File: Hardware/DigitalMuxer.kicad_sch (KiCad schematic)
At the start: 23 parts, among them SW1 Push_Button, SW2 Push_Button, SW3 Push_Button, SW4 Push_Button, SW5 Slide Switch, U2 PCF8574

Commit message: Use tags for nets, apply netgroups, mess around in pcb view
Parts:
- C10, C8, C9: footprint (none) -> Capacitor_SMD:C_0201_0603Metric
- D1, D2, D3: footprint (none) -> LED_SMD:LED_0201_0603Metric
- R10, R11, R12, R13, R3, R4, R5, R6, R7, R8, R9: footprint Resistor_THT:R_Axial_DIN0207_L6.3mm_D2.5mm_P10.16mm_Horizontal -> Resistor_SMD:R_0201_0603Metric
- U2: footprint (none) -> Snapeda:DW16
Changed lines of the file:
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@@
 			)
 		)
-		(property "Footprint" "Resistor_THT:R_Axial_DIN0207_L6.3mm_D2.5mm_P10.16mm_Horizontal"
+		(property "Footprint" "Resistor_SMD:R_0201_0603Metric"
 			(at 136.652 50.419 0)
 			(effects
@@
 			)
 		)
-		(property "Footprint" ""
+		(property "Footprint" "Snapeda:DW16"
 			(at 99.06 68.58 0)
 			(effects
@@
 			)
 		)
-		(property "Footprint" "Resistor_THT:R_Axial_DIN0207_L6.3mm_D2.5mm_P10.16mm_Horizontal"
+		(property "Footprint" "Resistor_SMD:R_0201_0603Metric"
 			(at 134.112 83.439 0)
 			(effects
@@
 			)
 		)
-		(property "Footprint" "Resistor_THT:R_Axial_DIN0207_L6.3mm_D2.5mm_P10.16mm_Horizontal"
+		(property "Footprint" "Resistor_SMD:R_0201_0603Metric"
 			(at 134.112 145.669 0)
 			(effects
@@
 			)
 		)
-		(property "Footprint" ""
+		(property "Footprint" "Capacitor_SMD:C_0201_0603Metric"
 			(at 111.4552 35.56 0)
 			(effects
@@
 			)
 		)
-		(property "Footprint" "Resistor_THT:R_Axial_DIN0207_L6.3mm_D2.5mm_P10.16mm_Horizontal"
+		(property "Footprint" "Resistor_SMD:R_0201_0603Metric"
 			(at 145.542 50.419 0)
 			(effects
@@
 			)
 		)
-		(property "Footprint" "Resistor_THT:R_Axial_DIN0207_L6.3mm_D2.5mm_P10.16mm_Horizontal"
+		(property "Footprint" "Resistor_SMD:R_0201_0603Metric"
 			(at 181.102 50.419 0)
 			(effects
@@
 			)
 		)
-		(property "Footprint" "Resistor_THT:R_Axial_DIN0207_L6.3mm_D2.5mm_P10.16mm_Horizontal"
+		(property "Footprint" "Resistor_SMD:R_0201_0603Metric"
 			(at 172.212 50.419 0)
 			(effects
@@
 			)
 		)
-		(property "Footprint" ""
+		(property "Footprint" "LED_SMD:LED_0201_0603Metric"
 			(at 172.72 60.96 90)
 			(effects
@@
 			)
 		)
-		(property "Footprint" ""
+		(property "Footprint" "Capacitor_SMD:C_0201_0603Metric"
 			(at 121.6152 35.56 0)
 			(effects
@@
 			)
 		)
-		(property "Footprint" "Resistor_THT:R_Axial_DIN0207_L6.3mm_D2.5mm_P10.16mm_Horizontal"
+		(property "Footprint" "Resistor_SMD:R_0201_0603Metric"
 			(at 154.432 50.419 0)
 			(effects
@@
 			)
 		)
-		(property "Footprint" "Resistor_THT:R_Axial_DIN0207_L6.3mm_D2.5mm_P10.16mm_Horizontal"
+		(property "Footprint" "Resistor_SMD:R_0201_0603Metric"
 			(at 134.112 98.679 0)
 			(effects
@@
 			)
 		)
-		(property "Footprint" "Resistor_THT:R_Axial_DIN0207_L6.3mm_D2.5mm_P10.16mm_Horizontal"
+		(property "Footprint" "Resistor_SMD:R_0201_0603Metric"
 			(at 134.112 113.919 0)
 			(effects
@@
 			)
 		)
-		(property "Footprint" "Resistor_THT:R_Axial_DIN0207_L6.3mm_D2.5mm_P10.16mm_Horizontal"
+		(property "Footprint" "Resistor_SMD:R_0201_0603Metric"
 			(at 163.322 50.419 0)
 			(effects
@@
 			)
 		)
-		(property "Footprint" "Resistor_THT:R_Axial_DIN0207_L6.3mm_D2.5mm_P10.16mm_Horizontal"
+		(property "Footprint" "Resistor_SMD:R_0201_0603Metric"
 			(at 134.112 130.429 0)
 			(effects
@@
 			)
 		)
-		(property "Footprint" ""
+		(property "Footprint" "LED_SMD:LED_0201_0603Metric"
 			(at 181.61 63.5 90)
 			(effects
@@
 			)
 		)
-		(property "Footprint" ""
+		(property "Footprint" "Capacitor_SMD:C_0201_0603Metric"
 			(at 102.5652 35.56 0)
 			(effects
@@
 			)
 		)
-		(property "Footprint" ""
+		(property "Footprint" "LED_SMD:LED_0201_0603Metric"
 			(at 163.83 58.42 90)
 			(effects

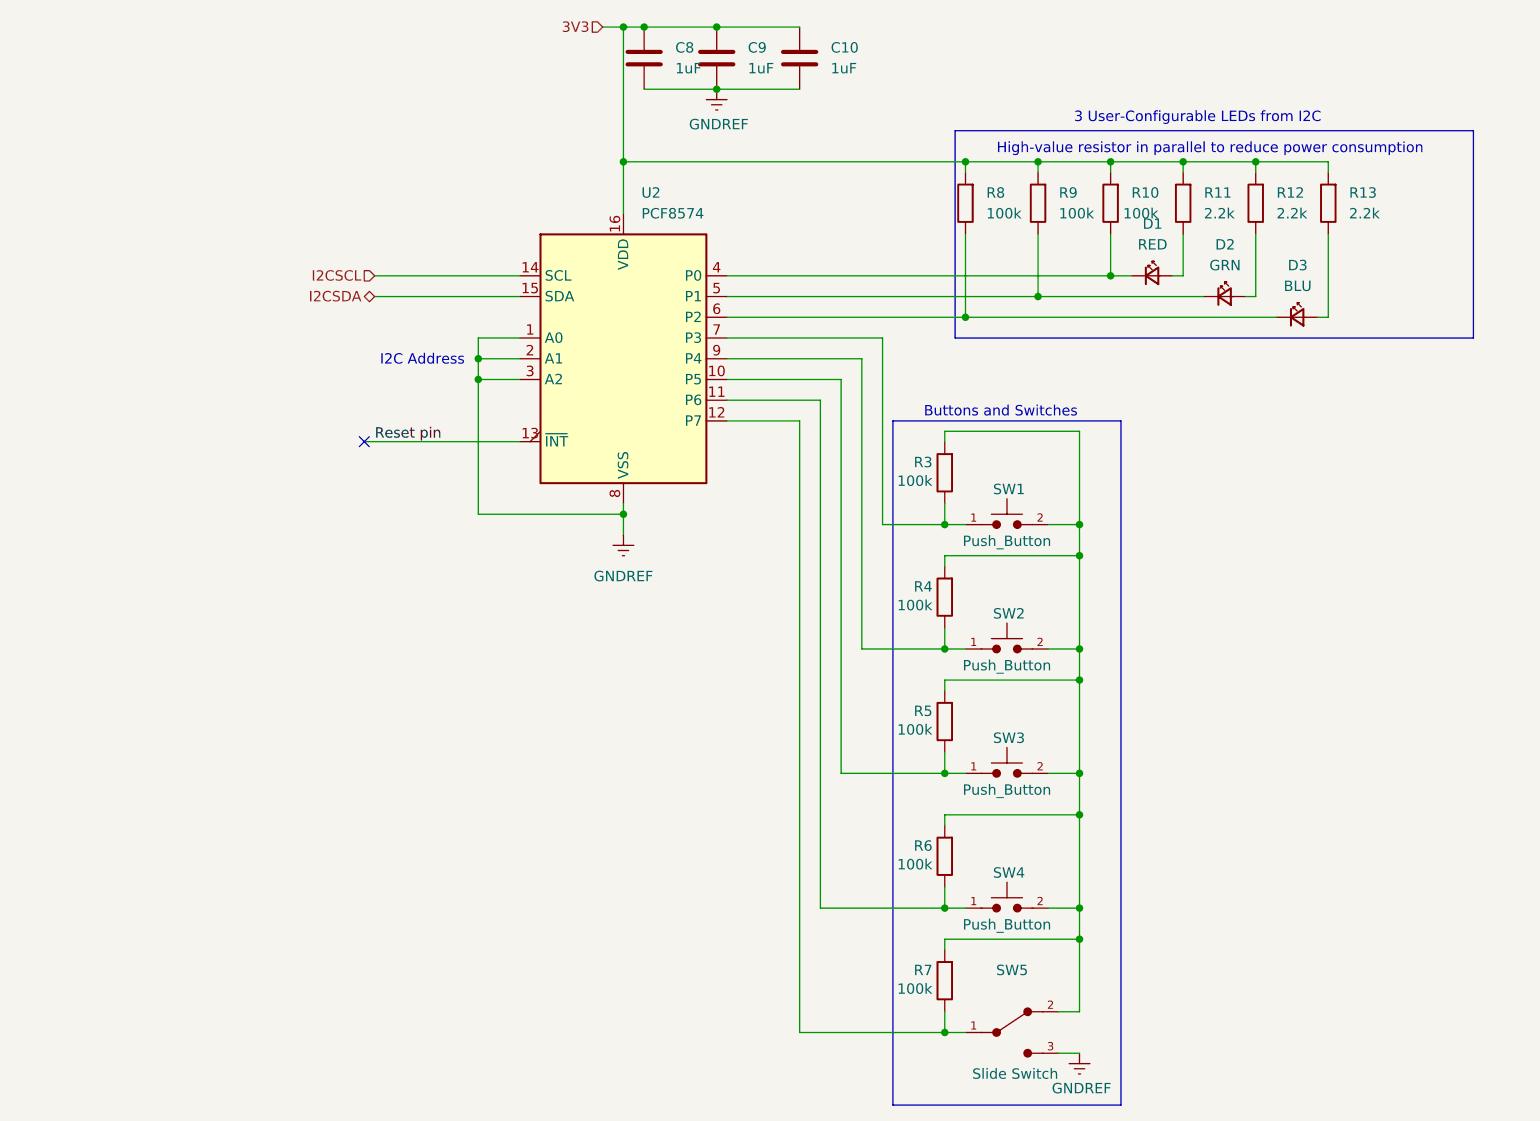
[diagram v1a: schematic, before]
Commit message: Use Peanut symbols, fix ERC errors, progress on DAC & Pressure
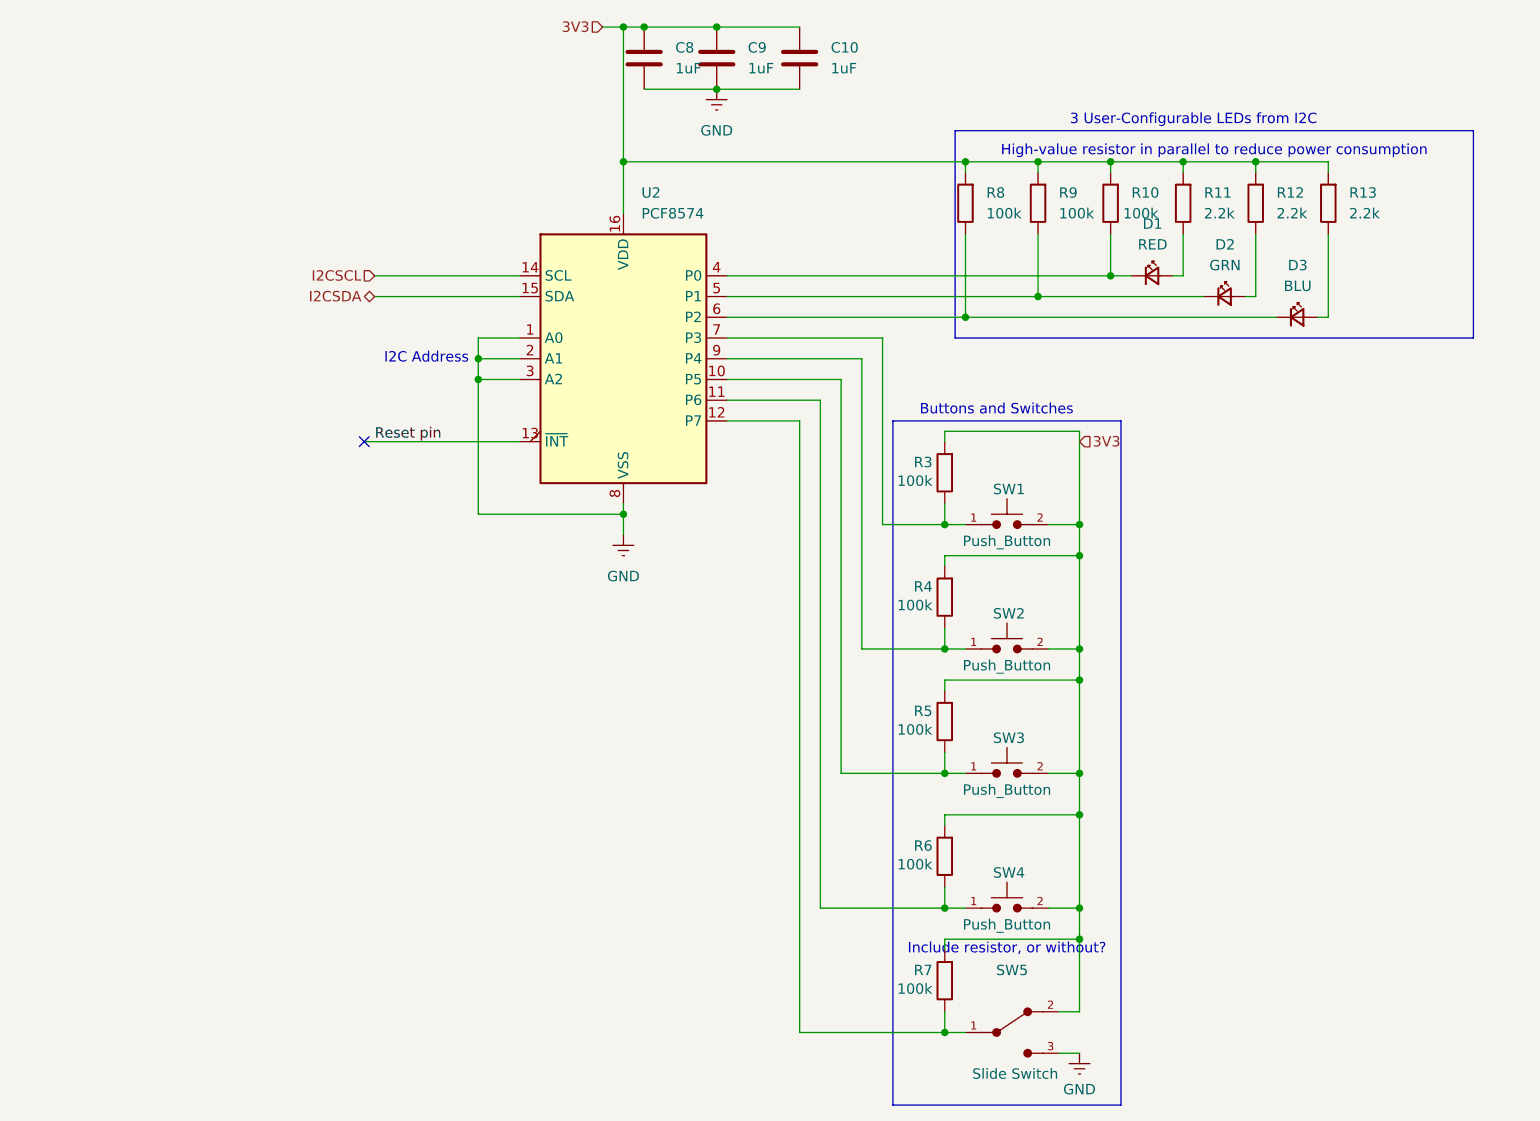
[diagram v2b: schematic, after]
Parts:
- R10, R11, R12, R13, R3, R4, R5, R6, R7, R8, R9: symbol PCM_SL_Resistors:2.2k -> Peanut:R
- SW1, SW2, SW3, SW4: footprint Button_Switch_THT:SW_PUSH_6mm -> Button_Switch_THT:SW_Tactile_SPST_Angled_PTS645Vx58-2LFS; symbol PCM_SL_Devices:Push_Button -> Peanut:Push_Button
- SW5: footprint PCM_SL_Devices:Slide_Switch_SPDT_P3mm_10x5x10mm -> Button_Switch_THT:SW_E-Switch_EG1224_SPDT_Angled; symbol PCM_SL_Devices:Slide_Switch_SPDT_P3mm_10x5x10mm -> Peanut:Slide_Switch_SPDT_P3mm_10x5x10mm
- U2: footprint Snapeda:DW16 -> Peanut:DW16
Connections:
- net 3V3: now also R3.1, R4.1, R5.1, R6.1, R7.1, SW1.2, SW2.2, SW3.2, SW4.2, SW5.2
- net GNDREF renamed GND
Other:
- note added: "Include resistor, or without?"

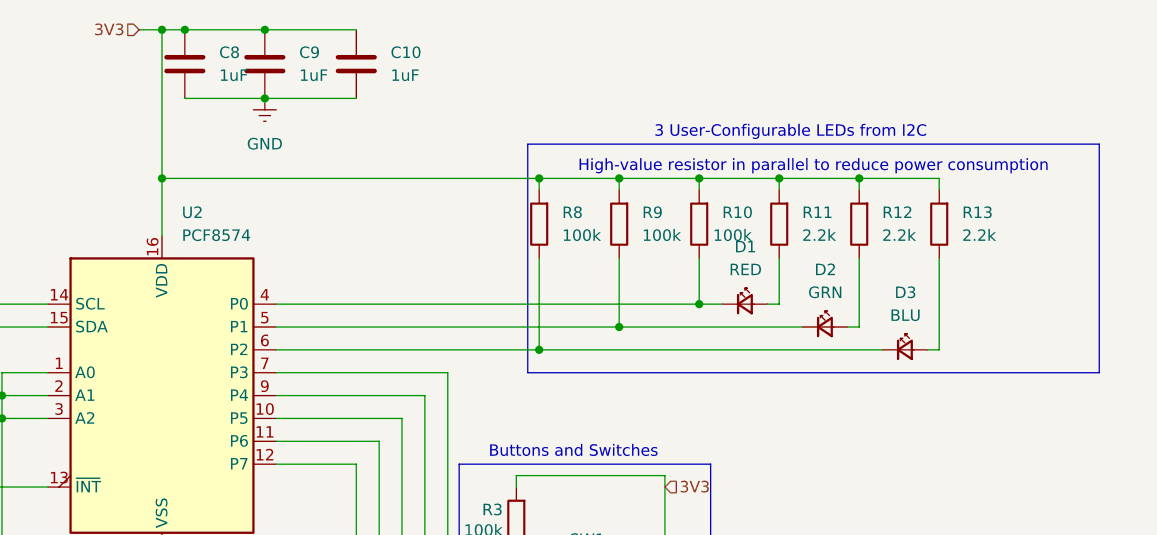
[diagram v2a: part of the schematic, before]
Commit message: Replace 1 LED with battery measurement toggle - We require an additional IO to toggle battery draining for % measurement, however we had no more ports. After a group discussion, one LED was dropped.
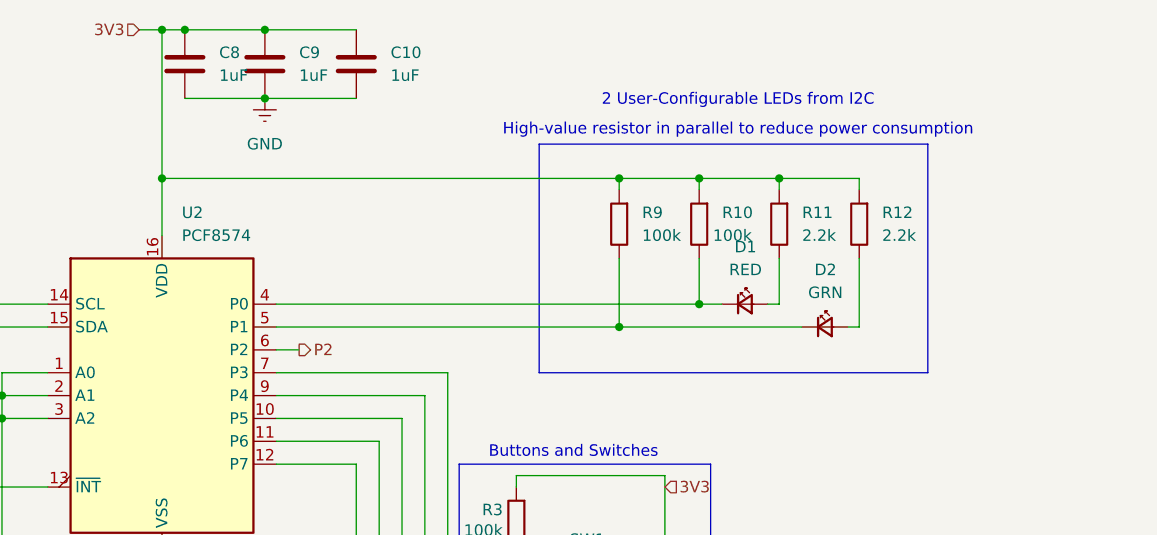
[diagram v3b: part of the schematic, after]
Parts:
- removed D3: BLU, LED_SMD:LED_0201_0603Metric, symbol PartsLib:LED_Small
- removed R13: 2.2k, Resistor_SMD:R_0201_0603Metric, symbol Peanut:R
- removed R8: 100k, Resistor_SMD:R_0201_0603Metric, symbol Peanut:R
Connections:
- net P2: now reaches U2.6 (P2)
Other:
- note added: "2 User-Configurable LEDs from I2C"
- note removed: "3 User-Configurable LEDs from I2C"

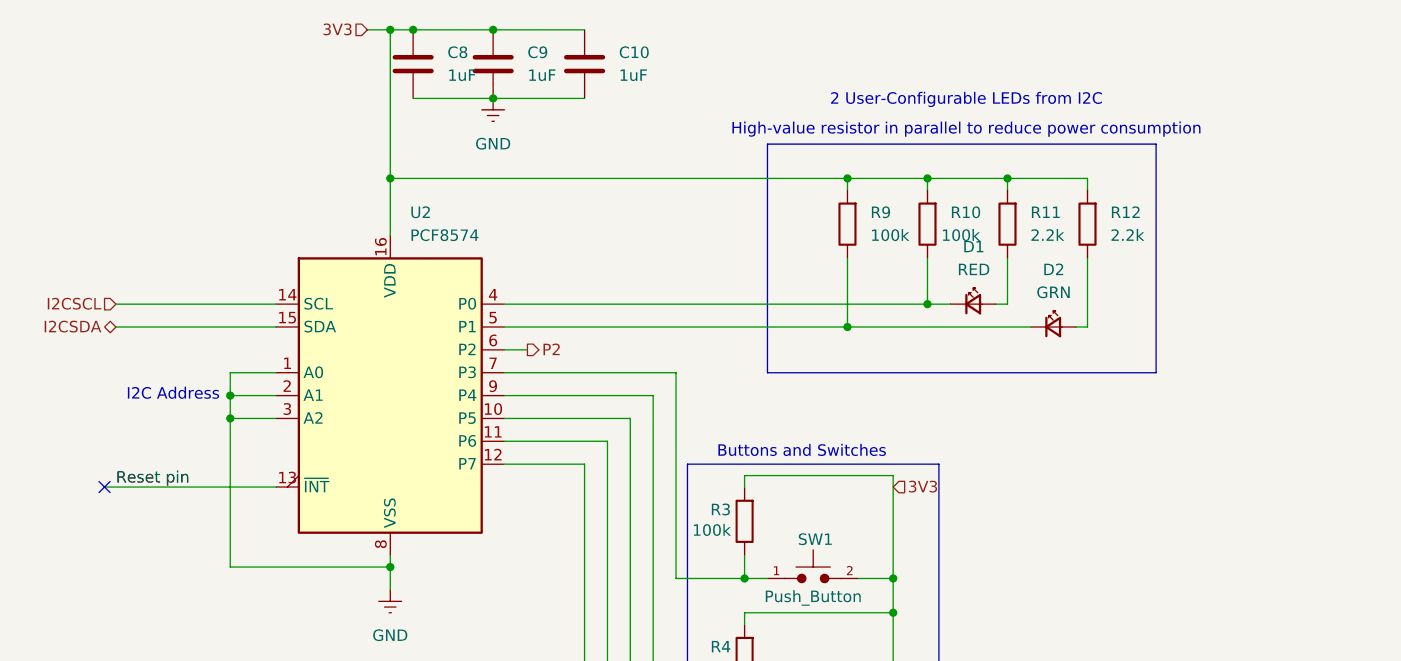
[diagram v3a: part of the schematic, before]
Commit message: Add Battery Monitoring & Use Project Parts Library
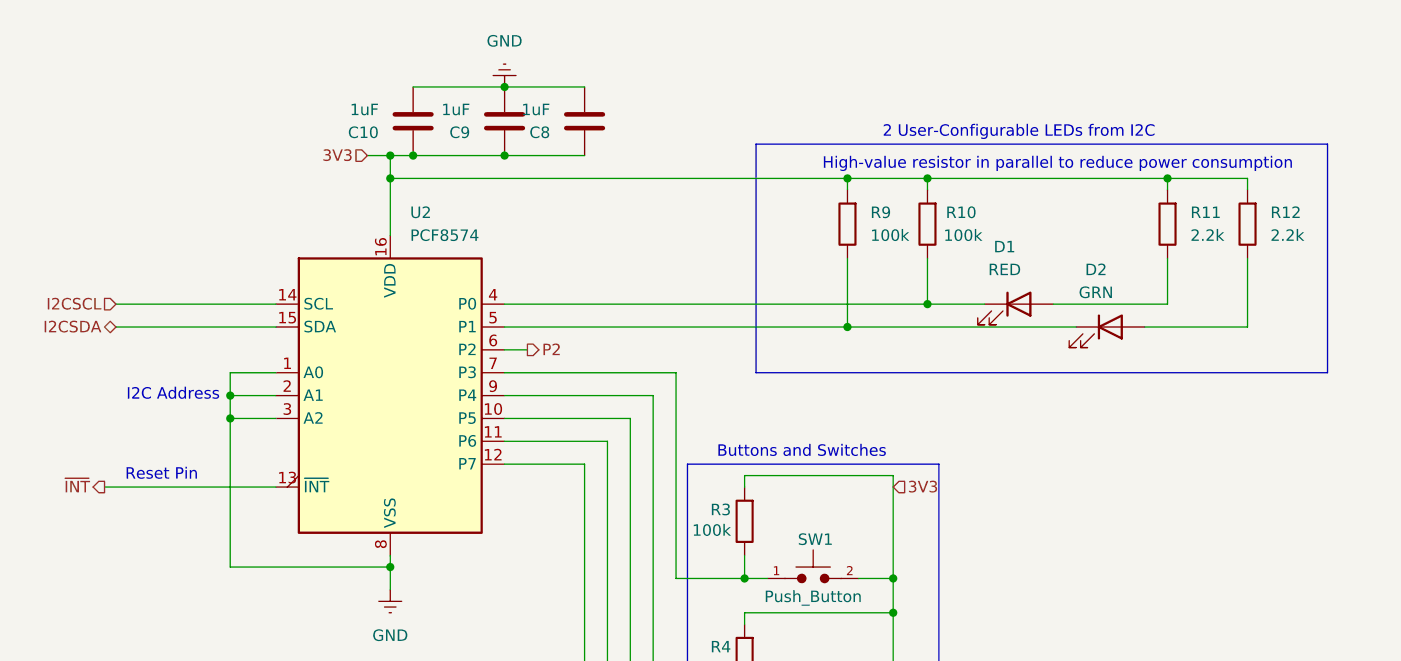
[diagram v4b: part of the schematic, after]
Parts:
- D1, D2: symbol PartsLib:LED_Small -> Peanut:LED
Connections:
- net Reset pin renamed ~{INT}
- no-connect marks 1 -> 0
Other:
- note added: "Reset Pin"
- moved on the sheet: C10, C8, C9, D1, D2, R11, R12

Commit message: Fully wired board!
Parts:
- removed U2: PCF8574, Peanut:DW16, symbol Interface_Expansion:PCF8574
- added U2: PCF8574APWR, Peanut:PW20, symbol Peanut:PCF8574APWR
- C10, C8, C9: footprint Capacitor_SMD:C_0201_0603Metric -> Resistor_SMD:R_01005_0402Metric; symbol Device:C -> Peanut:C
- R10, R11, R12, R3, R4, R5, R6, R7, R9: footprint Resistor_SMD:R_0201_0603Metric -> Resistor_SMD:R_0402_1005Metric
- SW5: footprint Button_Switch_THT:SW_E-Switch_EG1224_SPDT_Angled -> Peanut:SW-TH_SK12D07VG4
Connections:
- net 3V3: now also SW4.1, U2.5 (VCC); no longer SW4.2
- net GND: now also U2.15 (GND), U2.6 (A0), U2.7 (A1), U2.9 (A2)
- net I2CSCL: now also U2.2 (SCL)
- net I2CSDA: now also U2.4 (SDA)
- net P2: now also U2.10 (P0)
- net ~{INT}: now also U2.1 (*INT)
- net at R5.2, SW3.1: now also U2.11 (P1)
- net at R6.2: now also SW4.2, U2.12 (P2); no longer SW4.1
- net at R7.2, SW5.1: now also U2.17 (P5)
- net at D1.1 (K), R10.2: now also U2.19 (P6)
- net at D2.1 (K), R9.2: now also U2.20 (P7)
- net at R3.2, SW1.1: now also U2.16 (P4)
- net at R4.2, SW2.1: now also U2.14 (P3)
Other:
- note added: "Optimised for better PCB routing"
